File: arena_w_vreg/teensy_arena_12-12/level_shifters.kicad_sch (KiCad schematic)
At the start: 15 parts, among them U1 TXB0108PW, U2 TXB0108PW, U3 TXB0108PW, U4 TXB0108PW, U5 TXB0108PW

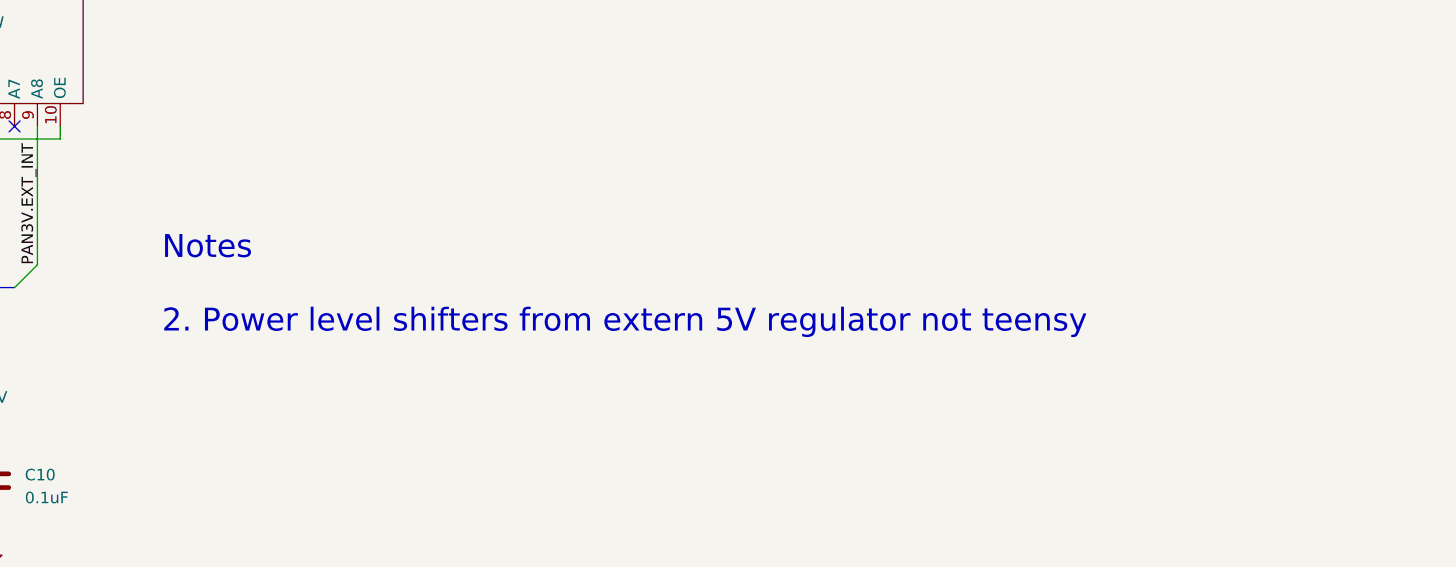
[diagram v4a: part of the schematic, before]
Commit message: Removed old notes from schematic pdf.
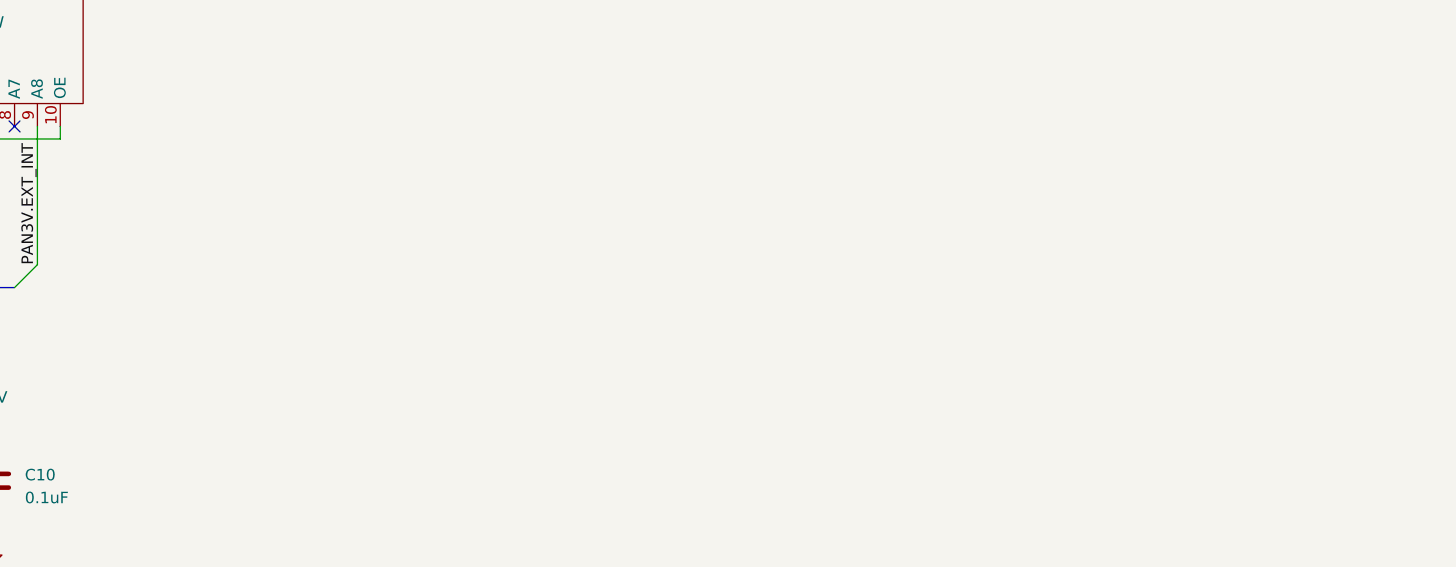
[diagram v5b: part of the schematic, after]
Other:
- note removed: "Notes 2. Power level shifters from extern 5V regulator not teensy"
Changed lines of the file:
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@@
     (stroke (width 0) (type default))
-  )
-  (text "Notes\n\n2. Power level shifters from extern 5V regulator not teensy\n"
-    (at 273.431 99.314 0)
-    (effects (font (size 2.54 2.54)) (justify left bottom))
   )
   (text "Level Shifters" (at 139.954 23.114 0)
